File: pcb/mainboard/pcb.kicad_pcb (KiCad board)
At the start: 4 copper layers, 89.5 x 88.5 mm, 40 parts, among them J10 Screw_Terminal_01x04, J11 Conn_01x02_Pin, J2 Screw_Terminal_01x04, J3 Screw_Terminal_01x02, J4 Screw_Terminal_01x03, J5 Screw_Terminal_01x03, J6 Screw_Terminal_01x07, J7 Screw_Terminal_01x02, J8 Conn_01x04_Pin, J9 Screw_Terminal_01x02, K1 SANYOU_SRD_Form_A, Q1 AO3400A, Q2 2N2222A, U1 ESP32-C6-MINI-1, U2 AMS1117-3.3, U3 AM2302

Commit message: making separate pcbs
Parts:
- removed C7: 10uF, Capacitor_THT:CP_Radial_D5.0mm_P2.00mm
- removed J1, J12: ~, Library:copper_pad 2x
- removed the REF** at (150.7, 43.5)
- removed the REF** at (79.0, 53.1)
- removed the REF** at (142.7, 43.5)
- added C5: 10uF, Capacitor_THT:CP_Radial_D5.0mm_P2.00mm, F.Cu at (109.1, 103.2)
- moved R8 90.2 mm to (93.8, 124.4), turned to 180 degrees
- moved R9 88.1 mm to (93.8, 122.9), turned to 180 degrees
- moved USB1 79.3 mm to (101.7, 123.9)
- moved C1 23.8 mm to (100.9, 80.9)
- moved C4 0.09 mm to (114.4, 119.6)
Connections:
- R8 pad 2: GND2 -> GND
- R9 pad 2: GND2 -> GND
- USB1 pad 7: GND2 -> GND
- USB1 pad A12: GND2 -> unconnected-(USB1-GND-PadA12)
- USB1 pad A9: Net-(J12-Pad2) -> +5V
- USB1 pad B12: GND2 -> unconnected-(USB1-GND-PadB12)
- USB1 pad B9: Net-(J12-Pad2) -> +5V
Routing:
- net Net-(J12-Pad2): track 16.8 -> 0.00 mm
- net GND2: track 9.60 -> 0.00 mm, vias 5 -> 0
- net Net-(USB1-CC2): track 4.38 -> 9.04 mm
- net Net-(USB1-CC1): track 4.58 -> 8.02 mm
- net +5V: track 39.3 -> 36.1 mm
- net GND: track 52.0 -> 49.4 mm, vias 66 -> 65
- removed copper zone on In1.Cu, net GND2

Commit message: generating the GERBERS
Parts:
- removed J10: Screw_Terminal_01x04, TerminalBlock_Phoenix:TerminalBlock_Phoenix_MKDS-1,5-4_1x04_P5.00mm_Horizontal
- removed R4: VT93xx, OptoDevice:R_LDR_4.9x4.2mm_P2.54mm_Vertical
- removed R5: 10k, Resistor_SMD:R_0603_1608Metric_Pad0.98x0.95mm_HandSolder
- removed U3: AM2302, Sensor:ASAIR_AM2302_P2.54mm_Lead2.75mm_TabDown
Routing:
- net VDD: track 34.0 -> 0.00 mm
- net GND1: track 26.7 -> 0.00 mm
- net Net-(J10-Pin_2): track 20.8 -> 0.00 mm
- net Net-(J10-Pin_3): track 19.2 -> 0.00 mm
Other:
- board size 89.5 x 88.5 mm -> 89.5 x 66.4 mm
- board text removed: "V cut"

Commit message: fixing some issues
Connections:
- J3 pad 2: +3.3V -> GND
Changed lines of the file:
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@@
 			(layers "*.Cu" "*.Mask")
 			(remove_unused_layers no)
-			(net "+3.3V")
+			(net "GND")
 			(pinfunction "Pin_2_2")
 			(pintype "passive")

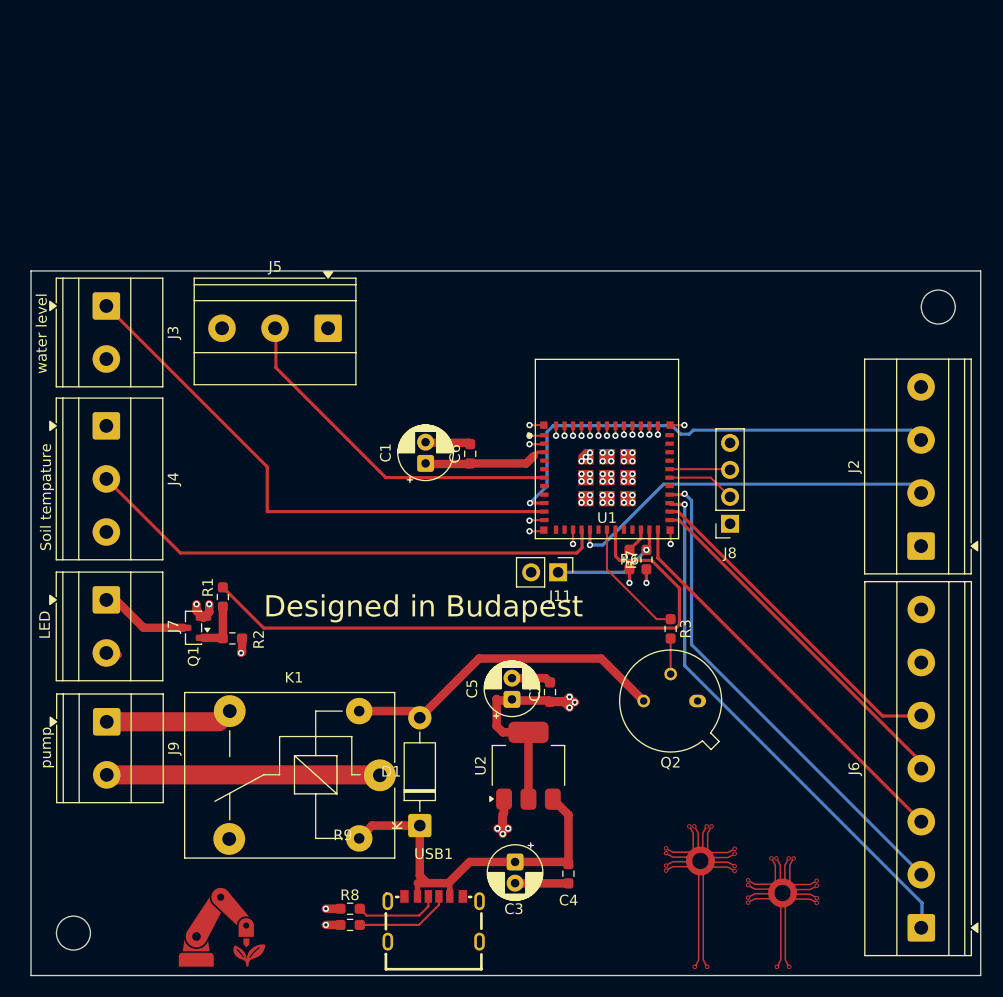
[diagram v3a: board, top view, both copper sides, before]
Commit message: fixed the problem with the bom
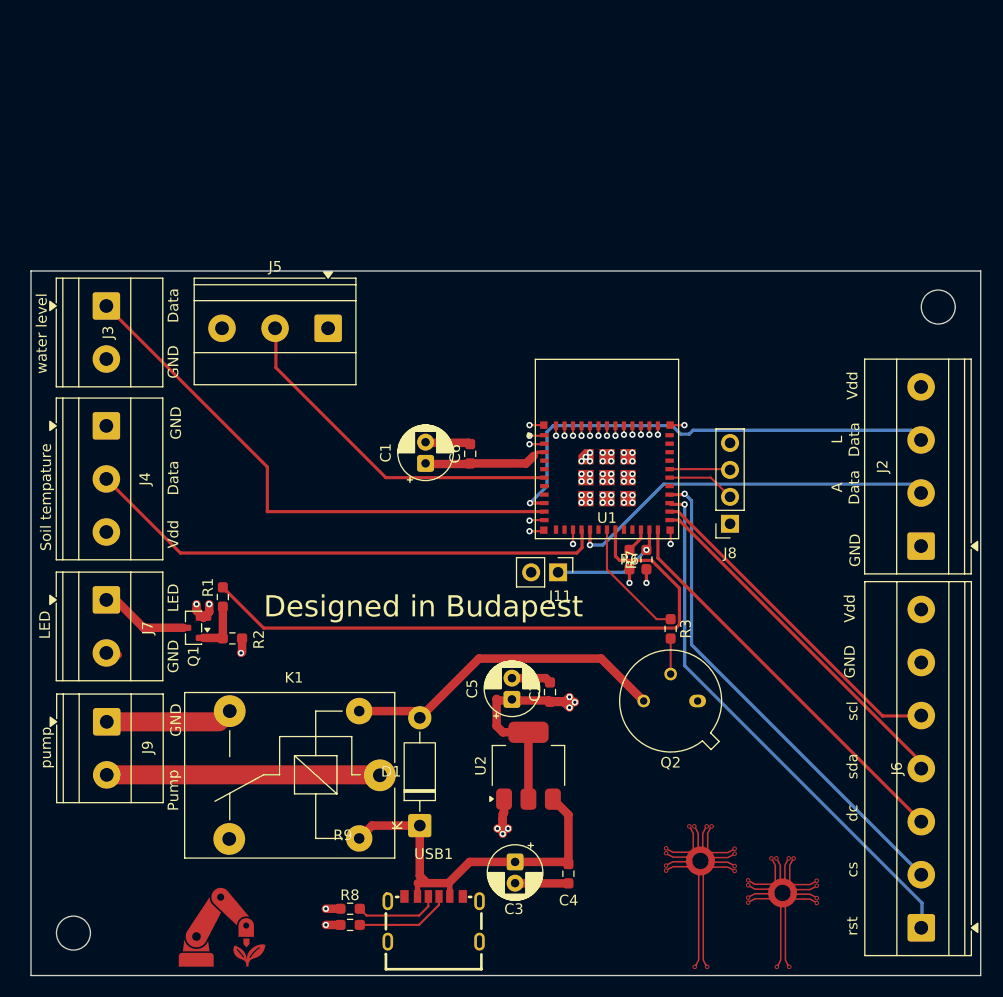
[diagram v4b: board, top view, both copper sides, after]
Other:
- board text added: "A Data"
- board text added: "Data"
- board text added: "GND"
- board text added: "L Data"
- board text added: "Pump"
- board text added: "Vdd"
- board text added: "cs"
- board text added: "dc"
- board text added: "rst"
- board text added: "scl"
- board text added: "sda"
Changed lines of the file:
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@@
 		(tags "THT Terminal Block Phoenix MKDS-1,5-3 pitch 5mm size 15x9.8mm drill 1.3mm pad 2.6mm")
 		(property "Reference" "J4"
-			(at 5 -6.32 90)
+			(at 5 -3.65 90)
 			(layer "F.SilkS")
 			(effects
@@
 			(at 5 5.72 90)
 			(layer "F.Fab")
+			(hide yes)
 			(effects
 				(font
@@
 		(tags "THT Terminal Block Phoenix MKDS-1,5-2 pitch 5mm size 10x9.8mm drill 1.3mm pad 2.6mm")
 		(property "Reference" "J3"
-			(at 2.5 -6.32 90)
+			(at 2.5 -0.1725 90)
 			(layer "F.SilkS")
 			(effects
@@
 			(at 18.349568 -13.528432 0)
 			(layer "F.Fab")
+			(hide yes)
 			(effects
 				(font
@@
 			(at 0.1375 5.1 90)
 			(layer "F.Fab")
+			(hide yes)
 			(effects
 				(font
@@
 		(tags "THT Terminal Block Phoenix MKDS-1,5-7 pitch 5mm size 35x9.8mm drill 1.3mm pad 2.6mm")
 		(property "Reference" "J6"
-			(at 15 -6.32 90)
+			(at 15 -2.3 90)
 			(layer "F.SilkS")
 			(effects
@@
 		(tags "THT Terminal Block Phoenix MKDS-1,5-4 pitch 5mm size 20x9.8mm drill 1.3mm pad 2.6mm")
 		(property "Reference" "J2"
-			(at 7.5 -6.32 90)
+			(at 7.5 -3.63 90)
 			(layer "F.SilkS")
 			(effects
@@
 		(tags "THT Terminal Block Phoenix MKDS-1,5-2 pitch 5mm size 10x9.8mm drill 1.3mm pad 2.6mm")
 		(property "Reference" "J9"
-			(at 2.5 -6.32 90)
+			(at 2.411 -3.86 90)
 			(layer "F.SilkS")
 			(effects
@@
 			(at 2.5 5.72 90)
 			(layer "F.Fab")
+			(hide yes)
 			(effects
 				(font
@@
 		(tags "THT Terminal Block Phoenix MKDS-1,5-2 pitch 5mm size 10x9.8mm drill 1.3mm pad 2.6mm")
 		(property "Reference" "J7"
-			(at 2.5 -6.32 90)
+			(at 2.65 -3.9 90)
 			(layer "F.SilkS")
 			(effects
@@
 			(at 2.5 5.72 90)
 			(layer "F.Fab")
+			(hide yes)
 			(effects
 				(font
@@
 		)
 	)
+	(gr_text "Data"
+		(at 77.739432 67.7 90)
+		(layer "F.SilkS")
+		(effects
+			(font
+				(size 1 1)
+				(thickness 0.1)
+			)
+			(justify left bottom)
+		)
+	)
+	(gr_text "GND"
+		(at 77.739432 72.95 90)
+		(layer "F.SilkS")
+		(effects
+			(font
+				(size 1 1)
+				(thickness 0.1)
+			)
+			(justify left bottom)
+		)
+	)
+	(gr_text "Data"
+		(at 77.739432 83.95 90)
+		(layer "F.SilkS")
+		(effects
+			(font
+				(size 1 1)
+				(thickness 0.1)
+			)
+			(justify left bottom)
+		)
+	)
+	(gr_text "Vdd"
+		(at 77.739432 88.95 90)
+		(layer "F.SilkS")
+		(effects
+			(font
+				(size 1 1)
+				(thickness 0.1)
+			)
+			(justify left bottom)
+		)
+	)
+	(gr_text "LED"
+		(at 77.739432 94.95 90)
+		(layer "F.SilkS")
+		(effects
+			(font
+				(size 1 1)
+				(thickness 0.1)
+			)
+			(justify left bottom)
+		)
+	)
+	(gr_text "GND"
+		(at 77.739432 100.7 90)
+		(layer "F.SilkS")
+		(effects
+			(font
+				(size 1 1)
+				(thickness 0.1)
+			)
+			(justify left bottom)
+		)
+	)
+	(gr_text "Pump"
+		(at 77.739432 113.7 90)
+		(layer "F.SilkS")
+		(effects
+			(font
+				(size 1 1)
+				(thickness 0.1)
+			)
+			(justify left bottom)
+		)
+	)
+	(gr_text "GND"
+		(at 77.989432 78.7 90)
+		(layer "F.SilkS")
+		(effects
+			(font
+				(size 1 1)
+				(thickness 0.1)
+			)
+			(justify left bottom)
+		)
+	)
+	(gr_text "GND"
+		(at 77.989432 106.7 90)
+		(layer "F.SilkS")
+		(effects
+			(font
+				(size 1 1)
+				(thickness 0.1)
+			)
+			(justify left bottom)
+		)
+	)
+	(gr_text "Vdd"
+		(at 141.489432 95.95 90)
+		(layer "F.SilkS")
+		(effects
+			(font
+				(size 1 1)
+				(thickness 0.1)
+			)
+			(justify left bottom)
+		)
+	)
+	(gr_text "GND"
+		(at 141.489432 101.2 90)
+		(layer "F.SilkS")
+		(effects
+			(font
+				(size 1 1)
+				(thickness 0.1)
+			)
+			(justify left bottom)
+		)
+	)
+	(gr_text "Vdd"
+		(at 141.739432 74.95 90)
+		(layer "F.SilkS")
+		(effects
+			(font
+				(size 1 1)
+				(thickness 0.1)
+			)
+			(justify left bottom)
+		)
+	)
+	(gr_text "scl"
+		(at 141.739432 105.2 90)
+		(layer "F.SilkS")
+		(effects
+			(font
+				(size 1 1)
+				(thickness 0.1)
+			)
+			(justify left bottom)
+		)
+	)
+	(gr_text "sda"
+		(at 141.739432 110.7 90)
+		(layer "F.SilkS")
+		(effects
+			(font
+				(size 1 1)
+				(thickness 0.1)
+			)
+			(justify left bottom)
+		)
+	)
+	(gr_text "dc"
+		(at 141.739432 114.7 90)
+		(layer "F.SilkS")
+		(effects
+			(font
+				(size 1 1)
+				(thickness 0.1)
+			)
+			(justify left bottom)
+		)
+	)
+	(gr_text "cs\n"
+		(at 141.739432 119.95 90)
+		(layer "F.SilkS")
+		(effects
+			(font
+				(size 1 1)
+				(thickness 0.1)
+			)
+			(justify left bottom)
+		)
+	)
+	(gr_text "rst"
+		(at 141.739432 125.45 90)
+		(layer "F.SilkS")
+		(effects
+			(font
+				(size 1 1)
+				(thickness 0.1)
+			)
+			(justify left bottom)
+		)
+	)
+	(gr_text "GND"
+		(at 141.989432 90.7 90)
+		(layer "F.SilkS")
+		(effects
+			(font
+				(size 1 1)
+				(thickness 0.1)
+			)
+			(justify left bottom)
+		)
+	)
+	(gr_text "L\nData"
+		(at 141.909432 78.7 90)
+		(layer "F.SilkS")
+		(effects
+			(font
+				(size 1 1)
+				(thickness 0.1)
+			)
+			(justify bottom)
+		)
+	)
+	(gr_text "A\nData"
+		(at 141.909432 83.2 90)
+		(layer "F.SilkS")
+		(effects
+			(font
+				(size 1 1)
+				(thickness 0.1)
+			)
+			(justify bottom)
+		)
+	)
 	(gr_text "Designed in Budapest"
 		(at 85.657932 95.6 0)
@@
 		(polygon
 			(pts
-				(xy 96.419432 76.679) (xy 96.439432 53) (xy 139.614432 58) (xy 139.619432 76.679)
+				(xy 96.419432 76.679) (xy 96.439432 53) (xy 139.614432 53.2) (xy 139.619432 76.679)
 			)
 		)

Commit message: adding silkscreen and finishin the main board
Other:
- board text added: "3.3V"
- board text added: "Boot"
- board text added: "humidity"
- board text added: "rx"
- board text added: "tx"
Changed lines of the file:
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@@
 		)
 		(property "Value" "ESP32-C6-MINI-1"
-			(at 0 6.9 0)
+			(at -0.03 -12.579 0)
 			(unlocked yes)
 			(layer "F.Fab")
@@
 		(tags "THT Terminal Block Phoenix MKDS-1,5-3 pitch 5mm size 15x9.8mm drill 1.3mm pad 2.6mm")
 		(property "Reference" "J5"
-			(at 4.980568 5.7985 0)
+			(at 5 -3.75 0)
 			(layer "F.SilkS")
 			(effects
@@
 		)
 		(property "Value" "Screw_Terminal_01x03"
-			(at 5 5.72 0)
+			(at 5 -6.5 0)
 			(layer "F.Fab")
 			(effects
@@
 		)
 		(fp_text user "${REFERENCE}"
-			(at 5 3.2 0)
+			(at 0 -3.75 0)
 			(layer "F.Fab")
 			(effects
@@
 		(tags "resistor handsolder")
 		(property "Reference" "C2"
-			(at 0 -1.43 90)
+			(at 4.2925 -3.91 180)
 			(layer "F.SilkS")
 			(effects
@@
 		(tags "resistor handsolder")
 		(property "Reference" "R6"
-			(at 0 0 180)
+			(at -3.2 1.85 180)
 			(layer "F.SilkS")
 			(effects
@@
 		(tags "resistor handsolder")
 		(property "Reference" "C6"
-			(at 0 -1.43 90)
+			(at 0.08 1.61 180)
 			(layer "F.SilkS")
 			(effects
@@
 		(tags "THT Terminal Block Phoenix MKDS-1,5-7 pitch 5mm size 35x9.8mm drill 1.3mm pad 2.6mm")
 		(property "Reference" "J6"
-			(at 15 -2.3 90)
+			(at 15.25 -3.4 90)
 			(layer "F.SilkS")
 			(effects
@@
 		)
 		(fp_text user "${REFERENCE}"
-			(at 0 3.81 90)
+			(at -1.8 -1.8 180)
 			(layer "F.Fab")
 			(effects
@@
 		(tags "Diode DO-41_SOD81 series Axial Horizontal pin pitch 10.16mm  length 5.2mm diameter 2.7mm")
 		(property "Reference" "D1"
-			(at 5.08 -2.7 0)
+			(at 5.119 2.36 0)
 			(layer "F.SilkS")
 			(effects
@@
 		)
 		(fp_text user "K"
-			(at 0 -2.1 90)
+			(at 0 2.11 0)
 			(layer "F.SilkS")
 			(effects
@@
 		(tags "resistor handsolder")
 		(property "Reference" "R9"
-			(at 0.676 6.925 0)
+			(at 0.072 1.706 0)
 			(layer "F.SilkS")
 			(effects
@@
 		(tags "Through hole pin header THT 1x02 2.54mm single row")
 		(property "Reference" "J11"
-			(at 2.242 -0.209 180)
+			(at -2.25 1.175 180)
 			(layer "F.SilkS")
 			(effects
@@
 		)
 		(property "Value" "Conn_01x02_Pin"
-			(at 0 4.92 90)
+			(at 2.25 0.675 180)
 			(layer "F.Fab")
 			(effects
@@
 		(tags "resistor handsolder")
 		(property "Reference" "R8"
-			(at 0.022 2.805 0)
+			(at 0.022 -1.77 0)
 			(layer "F.SilkS")
 			(effects
@@
 		(tags "resistor handsolder")
 		(property "Reference" "R7"
-			(at 0 -1.43 90)
+			(at -3.2 -1.75 180)
 			(layer "F.SilkS")
 			(effects
@@
 		(layer "Edge.Cuts")
 	)
+	(gr_text "Vdd"
+		(at 80.489432 76.45 0)
+		(layer "F.SilkS")
+		(effects
+			(font
+				(size 1 1)
+				(thickness 0.1)
+			)
+			(justify left bottom)
+		)
+	)
+	(gr_text "humidity"
+		(at 84.239432 78.45 0)
+		(layer "F.SilkS")
+		(effects
+			(font
+				(size 1 1)
+				(thickness 0.1)
+			)
+			(justify left bottom)
+		)
+	)
+	(gr_text "Data"
+		(at 85.489432 76.45 0)
+		(layer "F.SilkS")
+		(effects
+			(font
+				(size 1 1)
+				(thickness 0.1)
+			)
+			(justify left bottom)
+		)
+	)
+	(gr_text "GND"
+		(at 90.739432 76.45 0)
+		(layer "F.SilkS")
+		(effects
+			(font
+				(size 1 1)
+				(thickness 0.1)
+			)
+			(justify left bottom)
+		)
+	)
+	(gr_text "Boot"
+		(at 105.739432 91.7 0)
+		(layer "F.SilkS")
+		(effects
+			(font
+				(size 1 1)
+				(thickness 0.1)
+			)
+			(justify left bottom)
+		)
+	)
+	(gr_text "GND\n"
+		(at 131.419432 87.2 0)
+		(layer "F.SilkS")
+		(effects
+			(font
+				(size 1 1)
+				(thickness 0.1)
+			)
+			(justify left bottom)
+		)
+	)
+	(gr_text "3.3V"
+		(at 131.489432 79.7 0)
+		(layer "F.SilkS")
+		(effects
+			(font
+				(size 1 1)
+				(thickness 0.1)
+			)
+			(justify left bottom)
+		)
+	)
+	(gr_text "tx"
+		(at 131.489432 82.2 0)
+		(layer "F.SilkS")
+		(effects
+			(font
+				(size 1 1)
+				(thickness 0.1)
+			)
+			(justify left bottom)
+		)
+	)
+	(gr_text "rx"
+		(at 131.489432 84.7 0)
+		(layer "F.SilkS")
+		(effects
+			(font
+				(size 1 1)
+				(thickness 0.1)
+			)
+			(justify left bottom)
+		)
+	)
 	(gr_text "water level"
 		(at 65.339432 72.5 90)
@@
 	)
 	(gr_text "pump"
-		(at 65.739432 109.7 90)
+		(at 65.739432 110.2 90)
 		(layer "F.SilkS")
 		(effects
@@
 	)
 	(segment
-		(start 100.379432 119.8015)
-		(end 100.923432 120.3455)
-		(width 0.8)
-		(layer "F.Cu")
-		(net "+5V")
-	)
-	(segment
 		(start 100.185432 120.4955)
 		(end 103.076932 120.4955)
@@
 	)
 	(segment
+		(start 100.379432 115.069)
+		(end 100.379432 120.3015)
+		(width 0.8)
+		(layer "F.Cu")
+		(net "+5V")
+	)
+	(segment
 		(start 114.385432 114.045)
 		(end 112.919432 112.579)
@@
 	)
 	(segment
+		(start 100.379432 120.3015)
+		(end 100.185432 120.4955)
+		(width 0.8)
+		(layer "F.Cu")
+		(net "+5V")
+	)
+	(segment
 		(start 95.879432 115.069)
 		(end 94.669432 116.279)
@@
 		(layer "F.Cu")
 		(net "+5V")
-	)
-	(segment
-		(start 100.379432 115.069)
-		(end 100.379432 119.8015)
-		(width 0.8)
-		(layer "F.Cu")
-		(net "+5V")
